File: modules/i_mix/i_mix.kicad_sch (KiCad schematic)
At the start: 31 parts, among them U1 MCP6002-xSN, U2 MCP6002-xSN, U3 MCP6002-xSN

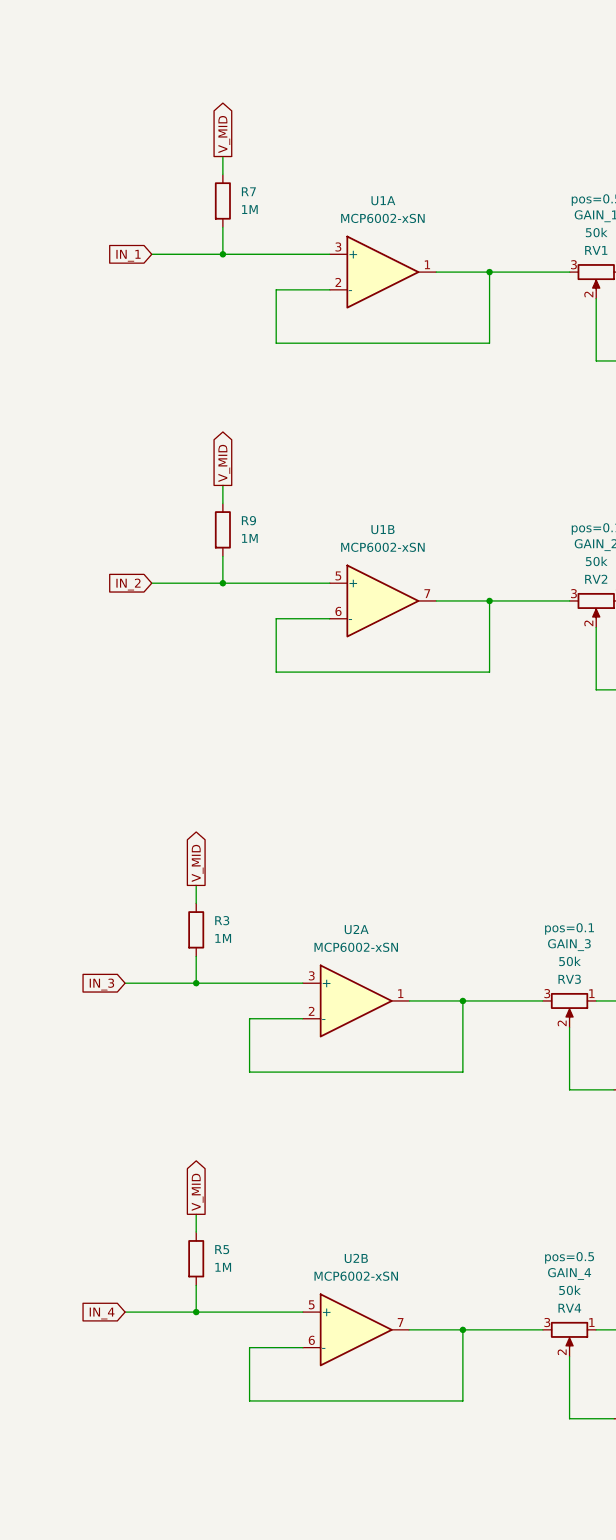
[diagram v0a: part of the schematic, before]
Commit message: i_mix: Use inverting buffers This will reducing picking up noise coming from cables
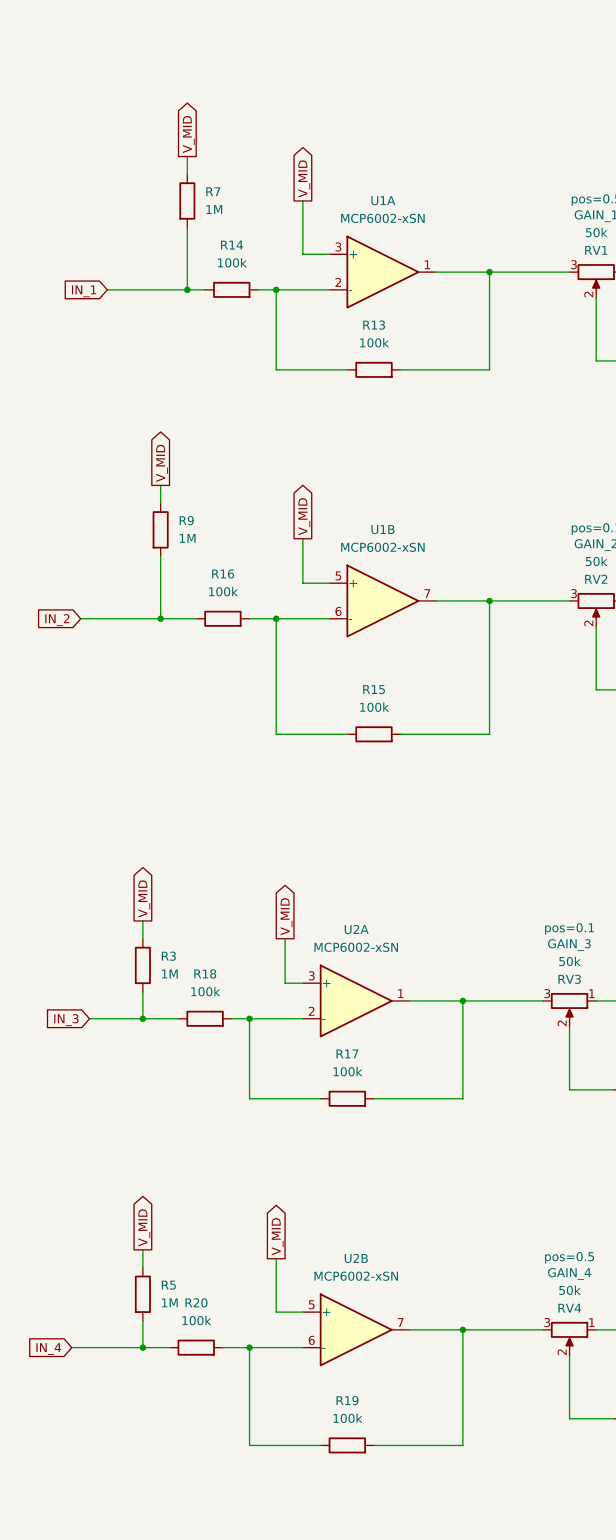
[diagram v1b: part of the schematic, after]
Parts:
- added R13, R14, R15, R16, R17, R18, R19, R20: 100k, Resistor_SMD:R_0402_1005Metric, symbol Device:R
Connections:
- net IN_1: now also R14.1; no longer U1.3 (+)
- net IN_2: now also R16.1; no longer U1.5 (+)
- net IN_3: now also R18.1; no longer U2.3 (+)
- net IN_4: now also R20.1; no longer U2.5 (+)
- net V_MID: now also U1.3 (+), U1.5 (+), U2.3 (+), U2.5 (+)
- net at RV3.3, U2.1: now also R17.2; no longer U2.2 (-)
- net at RV4.3, U2.7: now also R19.2; no longer U2.6 (-)
- net at RV1.3, U1.1: now also R13.2; no longer U1.2 (-)
- net at RV2.3, U1.7: now also R15.2; no longer U1.6 (-)
- new net: R19.1, R20.2, U2.6 (-)
- new net: R15.1, R16.2, U1.6 (-)
- new net: R17.1, R18.2, U2.2 (-)
- new net: R13.1, R14.2, U1.2 (-)
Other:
- moved on the sheet: R3, R5, R7, R9
